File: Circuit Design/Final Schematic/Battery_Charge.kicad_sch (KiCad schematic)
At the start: 10 parts

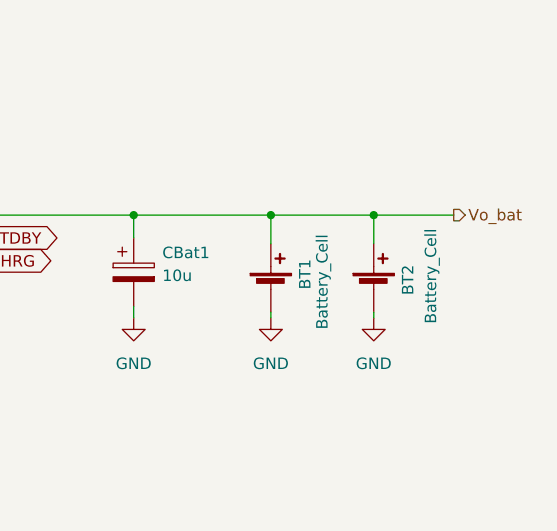
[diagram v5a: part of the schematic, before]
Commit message: Mejor ruteo xd Felipe cambie las huellas
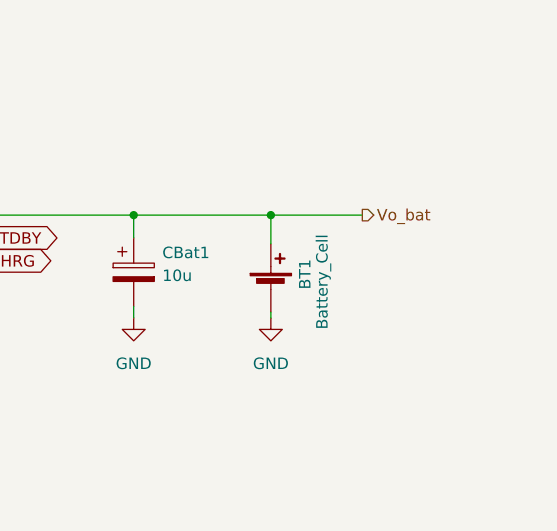
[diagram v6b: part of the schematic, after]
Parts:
- removed BT2: Battery_Cell, Battery:BatteryHolder_MPD_BH-18650-PC2, symbol Device:Battery_Cell
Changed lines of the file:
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@@
   (junction (at 147.32 79.375) (diameter 0) (color 0 0 0 0)
   )
-  (junction (at 207.645 97.155) (diameter 0) (color 0 0 0 0)
-  )
   (no_connect (at 161.925 107.315))
-  (wire (pts (xy 207.645 97.155) (xy 216.535 97.155))
-    (stroke (width 0) (type default) (color 0 0 0 0))
-  )
   (wire (pts (xy 180.975 97.155) (xy 180.975 99.695))
     (stroke (width 0) (type default) (color 0 0 0 0))
@@
     (stroke (width 0) (type default) (color 0 0 0 0))
   )
-  (wire (pts (xy 196.215 97.155) (xy 207.645 97.155))
+  (wire (pts (xy 196.215 97.155) (xy 206.375 97.155))
     (stroke (width 0) (type default) (color 0 0 0 0))
   )
@@
     (stroke (width 0) (type default) (color 0 0 0 0))
   )
-  (wire (pts (xy 207.645 107.95) (xy 207.645 108.585))
-    (stroke (width 0) (type default) (color 0 0 0 0))
-  )
   (wire (pts (xy 161.925 112.395) (xy 163.83 112.395))
     (stroke (width 0) (type default) (color 0 0 0 0))
@@
   )
   (wire (pts (xy 128.27 118.11) (xy 128.27 121.285))
-    (stroke (width 0) (type default) (color 0 0 0 0))
-  )
-  (wire (pts (xy 207.645 97.155) (xy 207.645 100.33))
     (stroke (width 0) (type default) (color 0 0 0 0))
   )
@@
     )
   )
-  (hierarchical_label "Vo_bat" (shape output) (at 216.535 97.155 0)
+  (hierarchical_label "Vo_bat" (shape output) (at 206.375 97.155 0)
     (effects (font (size 1.27 1.27)) (justify left))
   )
@@
     (pin "1")
   )
-  (symbol (lib_id "power:GND") (at 207.645 108.585 0) (unit 1)
-    (in_bom yes) (on_board yes) (fields_autoplaced)
-    (property "Reference" "#PWR0132" (id 0) (at 207.645 114.935 0)
-      (effects (font (size 1.27 1.27)) hide)
-    )
-    (property "Value" "GND" (id 1) (at 207.645 113.665 0))
-    (property "Footprint" "" (id 2) (at 207.645 108.585 0)
-      (effects (font (size 1.27 1.27)) hide)
-    )
-    (property "Datasheet" "" (id 3) (at 207.645 108.585 0)
-      (effects (font (size 1.27 1.27)) hide)
-    )
-    (pin "1")
-  )
   (symbol (lib_id "power:GND") (at 93.345 102.235 0) (unit 1)
     (in_bom yes) (on_board yes) (fields_autoplaced)
@@
     (pin "1")
   )
-  (symbol (lib_id "Device:Battery_Cell") (at 207.645 105.41 0) (unit 1)
-    (in_bom yes) (on_board yes)
-    (property "Reference" "BT2" (id 0) (at 211.455 106.045 90)
-      (effects (font (size 1.27 1.27)) (justify left))
-    )
-    (property "Value" "Battery_Cell" (id 1) (at 213.995 109.22 90)
-      (effects (font (size 1.27 1.27)) (justify left))
-    )
-    (property "Footprint" "Battery:BatteryHolder_MPD_BH-18650-PC2" (id 2) (at 207.645 103.886 90)
-      (effects (font (size 1.27 1.27)) hide)
-    )
-    (property "Datasheet" "~" (id 3) (at 207.645 103.886 90)
-      (effects (font (size 1.27 1.27)) hide)
-    )
-    (pin "1")
-    (pin "2")
-  )
   (symbol (lib_id "Device:LED") (at 116.84 104.14 90) (unit 1)

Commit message: More free space schematic
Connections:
- net 5v0: now also D_RED1.2 (A), U_ChargeControler1.8 (CE)
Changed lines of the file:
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@@
 (kicad_sch (version 20211123) (generator eeschema)
   (paper "A4")
+  (junction (at 116.84 79.375) (diameter 0) (color 0 0 0 0)
+  )
   (junction (at 196.215 97.155) (diameter 0) (color 0 0 0 0)
+  )
+  (junction (at 116.84 99.695) (diameter 0) (color 0 0 0 0)
   )
   (junction (at 106.045 79.375) (diameter 0) (color 0 0 0 0)
@@
   )
   (no_connect (at 161.925 107.315))
+  (wire (pts (xy 116.84 79.375) (xy 106.045 79.375))
+    (stroke (width 0) (type default) (color 0 0 0 0))
+  )
   (wire (pts (xy 180.975 97.155) (xy 180.975 99.695))
     (stroke (width 0) (type default) (color 0 0 0 0))
@@
     (stroke (width 0) (type default) (color 0 0 0 0))
   )
+  (wire (pts (xy 116.84 79.375) (xy 116.84 99.695))
+    (stroke (width 0) (type default) (color 0 0 0 0))
+  )
   (wire (pts (xy 131.445 97.155) (xy 128.27 97.155))
     (stroke (width 0) (type default) (color 0 0 0 0))
@@
     (stroke (width 0) (type default) (color 0 0 0 0))
   )
-  (wire (pts (xy 147.32 79.375) (xy 106.045 79.375))
+  (wire (pts (xy 147.32 79.375) (xy 116.84 79.375))
     (stroke (width 0) (type default) (color 0 0 0 0))
   )
